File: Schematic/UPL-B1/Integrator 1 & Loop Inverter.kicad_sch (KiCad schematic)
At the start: 103 parts, among them P30 TestPoint, P31 TestPoint, P32 TestPoint, P33 TestPoint, P34 TestPoint

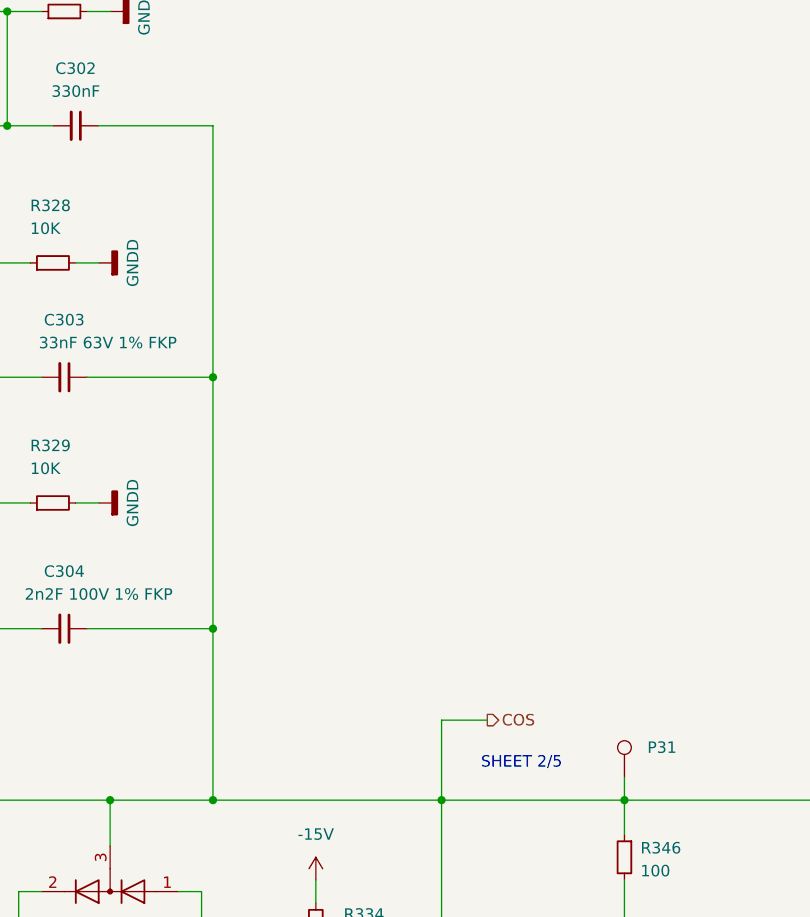
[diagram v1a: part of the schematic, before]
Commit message: Annotate with reverse engineering clues
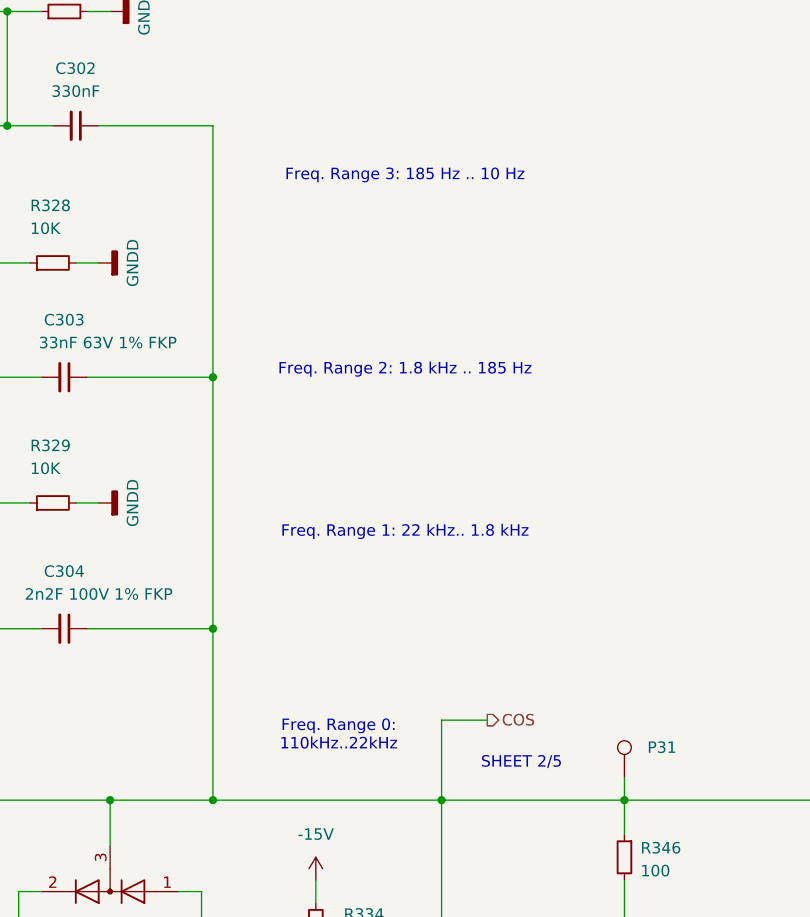
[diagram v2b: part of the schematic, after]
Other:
- note added: "Freq. Range 0: 110kHz..22kHz"
- note added: "Freq. Range 1: 22 kHz.. 1.8 kHz"
- note added: "Freq. Range 2: 1.8 kHz .. 185 Hz"
- note added: "Freq. Range 3: 185 Hz .. 10 Hz"
